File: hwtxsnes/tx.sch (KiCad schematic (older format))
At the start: 39 parts, among them IC1 ATMEGA328-A, J1 POWER_JACK, P1 nRF, P2 ISP, P3 bLT+, P4 bLT-, P5 bRT+, P6 bRT-, P7 SER_RX, P8 SER_TX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

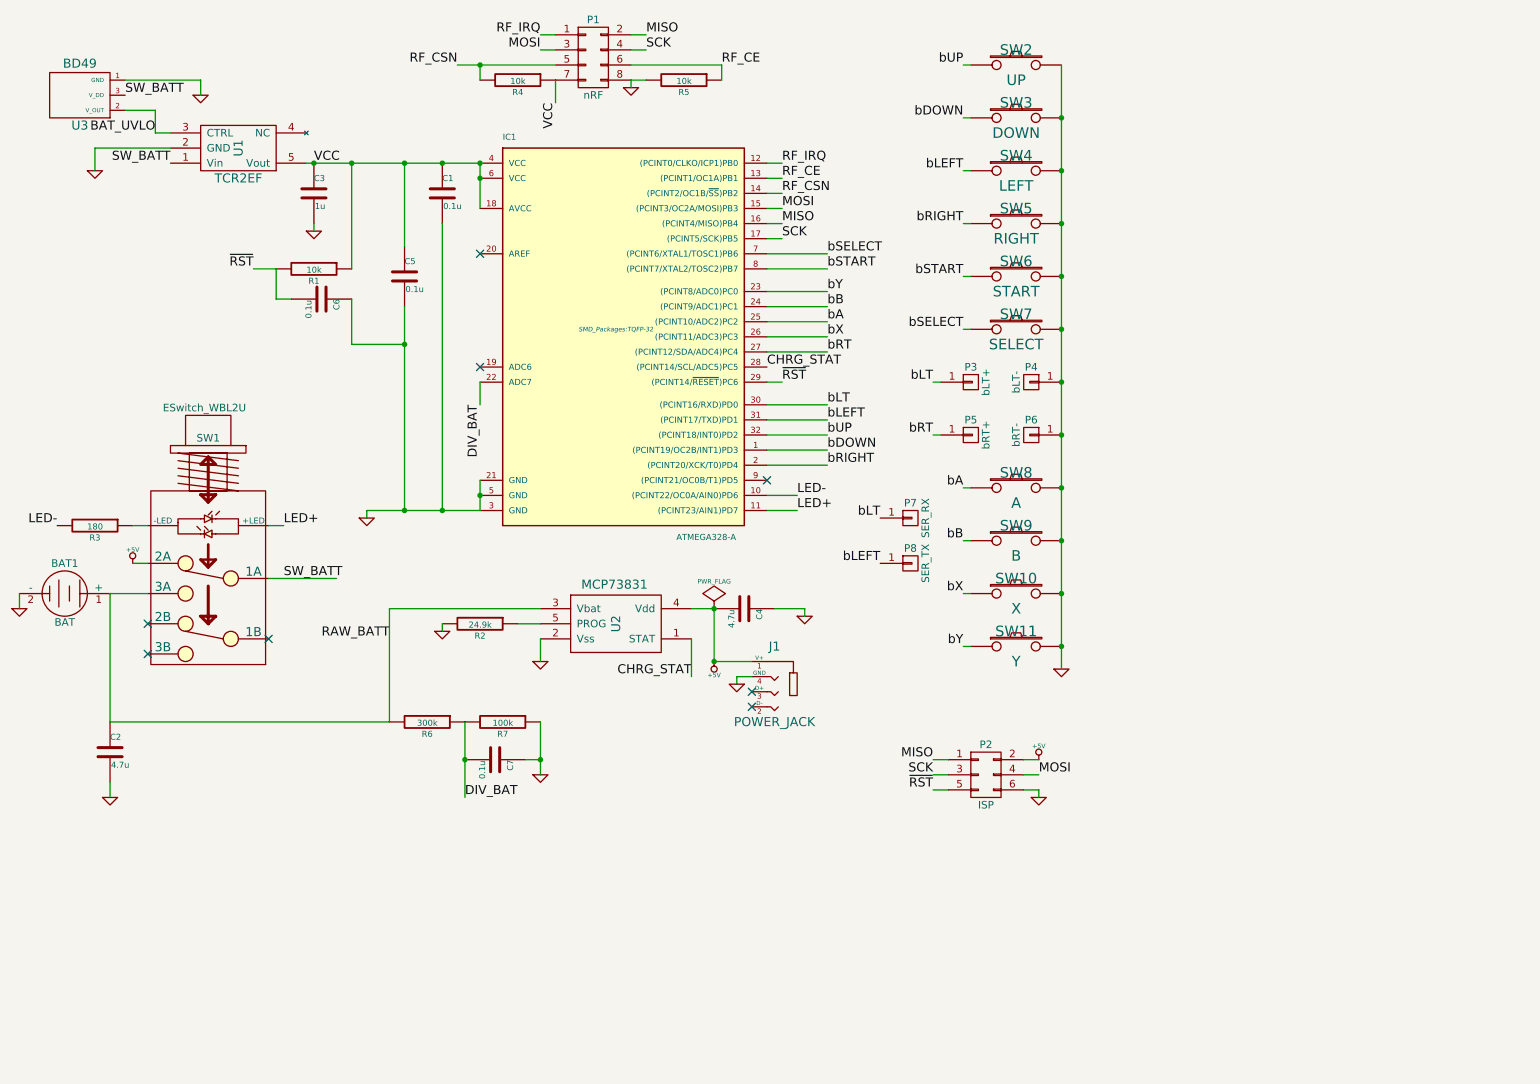
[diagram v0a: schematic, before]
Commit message: v2
* Schematic revs:
  * TVS protection on TX
  * TX voltage divider moved after the power switch
  * RX adds crystal to run at 16MHz
RX software tested w/ a real console.
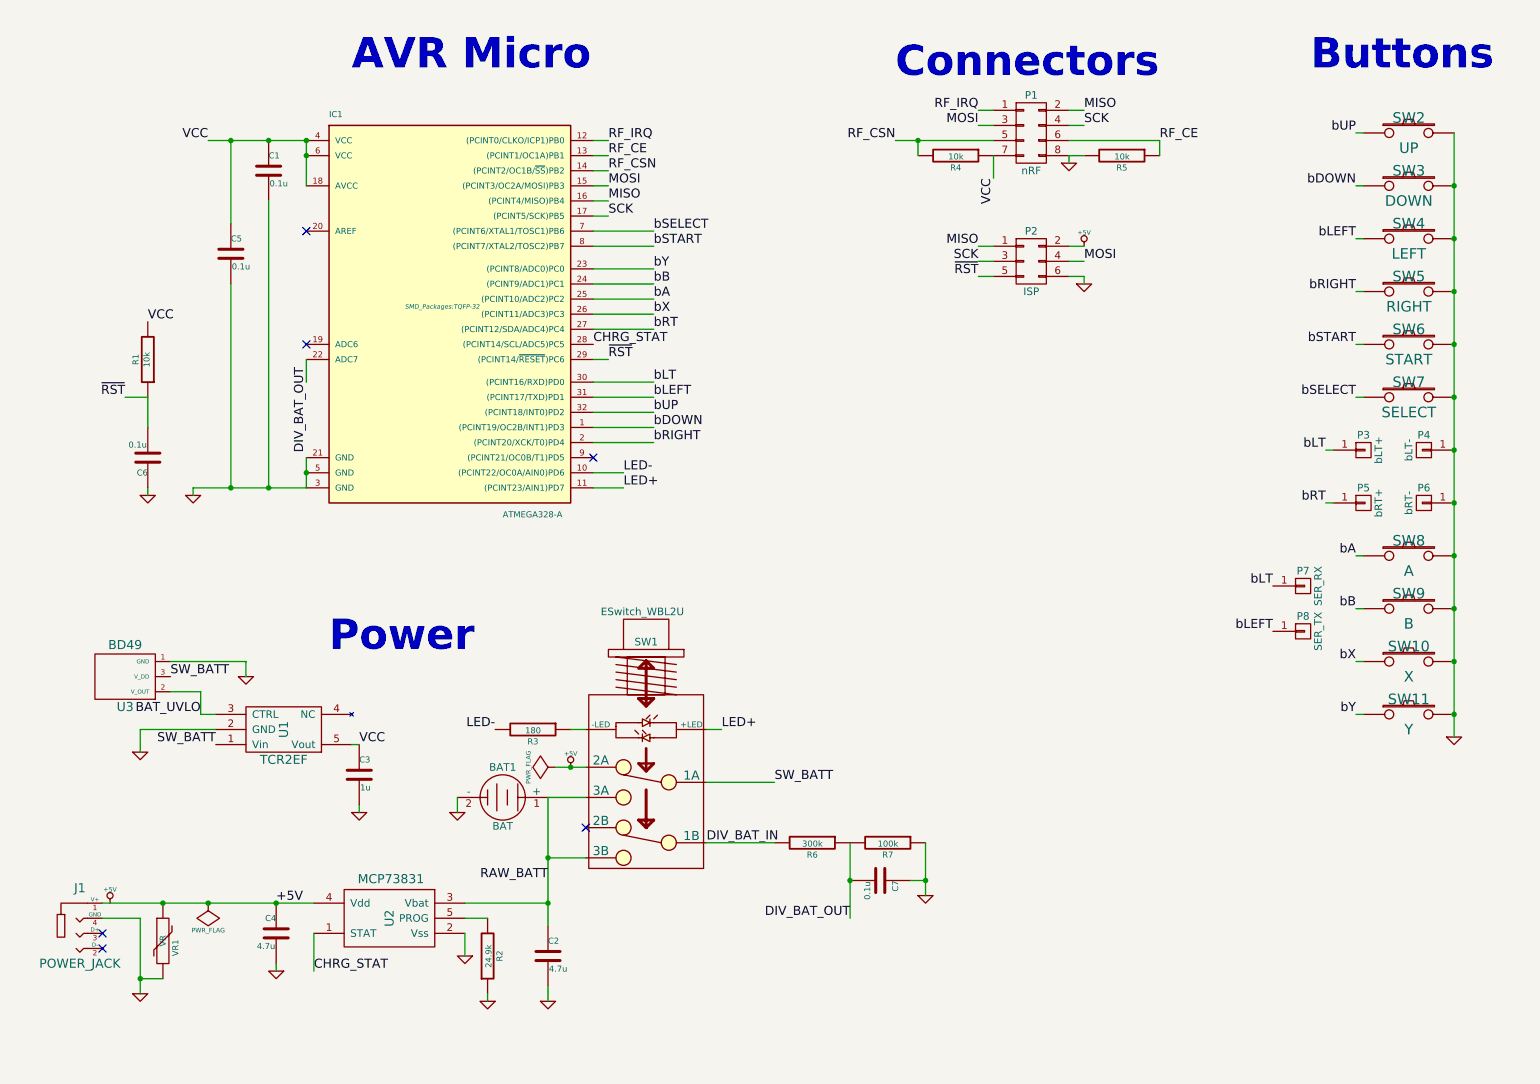
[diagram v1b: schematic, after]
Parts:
- added VR1: VR, SMD_Packages:SMD-0603, symbol VR
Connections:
- net +5V: now also C4.1, VR1.1; no longer C4.2
- net GND: now also C4.2, R2.1, VR1.2; no longer C4.1, R2.2
- net RAW_BATT: now also SW1.6 (3B); no longer R6.2
- net VCC: now also R1.2; no longer R1.1
- net ~RST: now also R1.1; no longer R1.2
- net at U2.5 (PROG): now also R2.2; no longer R2.1
- net DIV_BAT_IN: now reaches SW1.5 (1B)
- net DIV_BAT_IN: now also R6.2
- net DIV_BAT renamed DIV_BAT_OUT
- no-connect marks 8 -> 6
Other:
- note added: "AVR Micro"
- note added: "Buttons"
- note added: "Connectors"
- note added: "Power"
- moved on the sheet: BAT1, C1, C2, C3, C4, C5, C6, C7, IC1, J1, P1, P2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

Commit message: end-to-end working on breadboard
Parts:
- added R8: 10k, SMD_Packages:SMD-0402_r, symbol R
- P1: footprint Pin_Headers:Pin_Header_Straight_2x04 -> nesRF TX:nRF_Header_2x04
- P3, P4, P5, P6, P7, P8: footprint Wire_Pads:SolderWirePad_single_1mmDrill -> Wire_Pads:SolderWirePad_single_0-8mmDrill
- R2: value 24.9k -> 19.1k
- U2: value MCP73831 -> MCP73832
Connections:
- net CHRG_STAT: now also IC1.9 ((PCINT21/OC0B/T1)PD5), R8.2; no longer IC1.28 ((PCINT14/SCL/ADC5)PC5)
- net LED+: now also IC1.10 ((PCINT22/OC0A/AIN0)PD6); no longer IC1.11 ((PCINT23/AIN1)PD7)
- net LED-: now also IC1.11 ((PCINT23/AIN1)PD7); no longer IC1.10 ((PCINT22/OC0A/AIN0)PD6)
- net RF_CE: now also IC1.14 ((PCINT2/OC1B/~SS~)PB2); no longer IC1.13 ((PCINT1/OC1A)PB1)
- net RF_CSN: now also IC1.13 ((PCINT1/OC1A)PB1); no longer IC1.14 ((PCINT2/OC1B/~SS~)PB2)
- net RF_IRQ: now also IC1.32 ((PCINT18/INT0)PD2); no longer IC1.12 ((PCINT0/CLKO/ICP1)PB0)
- net VCC: now also R8.1
- net bA: now also IC1.2 ((PCINT20/XCK/T0)PD4); no longer IC1.25 ((PCINT10/ADC2)PC2)
- net bB: now also IC1.1 ((PCINT19/OC2B/INT1)PD3); no longer IC1.24 ((PCINT9/ADC1)PC1)
- net bDOWN: now also IC1.30 ((PCINT16/RXD)PD0), P7.1 (P1); no longer IC1.1 ((PCINT19/OC2B/INT1)PD3)
- net bLEFT: now also IC1.28 ((PCINT14/SCL/ADC5)PC5); no longer IC1.31 ((PCINT17/TXD)PD1), P8.1 (P1)
- net bLT: now also IC1.27 ((PCINT12/SDA/ADC4)PC4); no longer IC1.30 ((PCINT16/RXD)PD0), P7.1 (P1)
- net bRIGHT: now also IC1.25 ((PCINT10/ADC2)PC2); no longer IC1.2 ((PCINT20/XCK/T0)PD4)
- net bRT: now also IC1.8 ((PCINT7/XTAL2/TOSC2)PB7); no longer IC1.27 ((PCINT12/SDA/ADC4)PC4)
- net bSELECT: now also IC1.24 ((PCINT9/ADC1)PC1); no longer IC1.7 ((PCINT6/XTAL1/TOSC1)PB6)
- net bSTART: now also IC1.23 ((PCINT8/ADC0)PC0); no longer IC1.8 ((PCINT7/XTAL2/TOSC2)PB7)
- net bUP: now also IC1.26 ((PCINT11/ADC3)PC3); no longer IC1.32 ((PCINT18/INT0)PD2)
- net bX: now also IC1.7 ((PCINT6/XTAL1/TOSC1)PB6); no longer IC1.26 ((PCINT11/ADC3)PC3)
- net bY: now also IC1.12 ((PCINT0/CLKO/ICP1)PB0); no longer IC1.23 ((PCINT8/ADC0)PC0)
- net CHRG_PROG: now reaches R2.2, U2.5 (PROG)
- net LED_LIMITER: now reaches R3.1, SW1.- (-LED)
- new net TX: IC1.31 ((PCINT17/TXD)PD1), P8.1 (P1)
- no-connect marks 6 -> 5
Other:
- moved on the sheet: BAT1, C4, J1, R2, U2, VR1
